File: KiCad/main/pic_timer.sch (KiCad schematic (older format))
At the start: 4 parts, among them U10 8254, U11 8259, U12 27C512, X1 1 MHz

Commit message: Updated graphics adapter and main schematics + board.
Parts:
- added R5: 4K7, Resistor_THT:R_Axial_DIN0207_L6.3mm_D2.5mm_P7.62mm_Horizontal, symbol Device:R
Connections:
- net VCC: now also R5.1; no longer U11.16 (~SP~/~EN~)
- net ~IO2 renamed ~IO_DBG
- new net: R5.2, U11.16 (~SP~/~EN~)
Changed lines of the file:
@@
 ~IO1
 Text GLabel 9550 3000 2    50   Output ~ 0
-~IO2
+~IO_DBG
 Text GLabel 9900 3100 2    50   Output ~ 0
 ~VGA_MEM
@@
 Text GLabel 6000 2350 2    50   Input ~ 0
 IRQ2
-Wire Wire Line
-	5900 3150 6250 3150
 Wire Wire Line
 	6250 3150 6250 3050
@@
 NoConn ~ 5900 2850
 NoConn ~ 5900 2950
+$Comp
+L Device:R R5
+U 1 1 5F78548B
+P 6100 3150
+F 0 "R5" V 5893 3150 50  0000 C CNN
+F 1 "4K7" V 5984 3150 50  0000 C CNN
+F 2 "Resistor_THT:R_Axial_DIN0207_L6.3mm_D2.5mm_P7.62mm_Horizontal" V 6030 3150 50  0001 C CNN
+F 3 "~" H 6100 3150 50  0001 C CNN
+	1    6100 3150
+	0    1    1    0
+$EndComp
+Wire Wire Line
+	5950 3150 5900 3150
 Wire Bus Line
 	2000 5800 2000 5950

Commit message: Updated KiCad VGA board and main board.
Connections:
- net IRQ2: now also U10.13 (OUT1)
- net IRQ0: now reaches U10.10 (OUT0), U11.18 (IR0)
- net IRQ1: now reaches U11.19 (IR1)
- net IRQ1: no longer U10.13 (OUT1)
- net NMI renamed TMR2
- net ~IO0 renamed ~IO_TIMER
- net ~IO1 renamed ~IO_PIC
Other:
- note added: "I/O decoder"
- moved on the sheet: R5, U10, U11, U12, X1

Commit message: Updated main system board schematics and board.
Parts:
- removed U12: 27C512, Package_DIP:DIP-28_W15.24mm_Socket_LongPads, symbol Memory_EPROM:27C512
- added R10, R11, R12, R13, R14, R9: 10K, Resistor_THT:R_Axial_DIN0207_L6.3mm_D2.5mm_P2.54mm_Vertical, symbol Device:R_Small
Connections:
- net A2 is gone; now on net A1: U10.20 (A1)
- net A1: no longer U10.19 (A0), U11.27 (A0)
- net GND: now also R10.2, R11.2, R12.2, R13.2, R14.2, R9.2
- net IRQ1: now also R9.1
- net IRQ3: now also R10.1
- net IRQ4: now also R11.1
- net IRQ5: now also R12.1
- net IRQ6: now also R13.1
- net IRQ7: now also R14.1
- new net A0: U10.19 (A0), U11.27 (A0)
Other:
- note removed: "I/O decoder"
- moved on the sheet: R5, U10, U11, X1

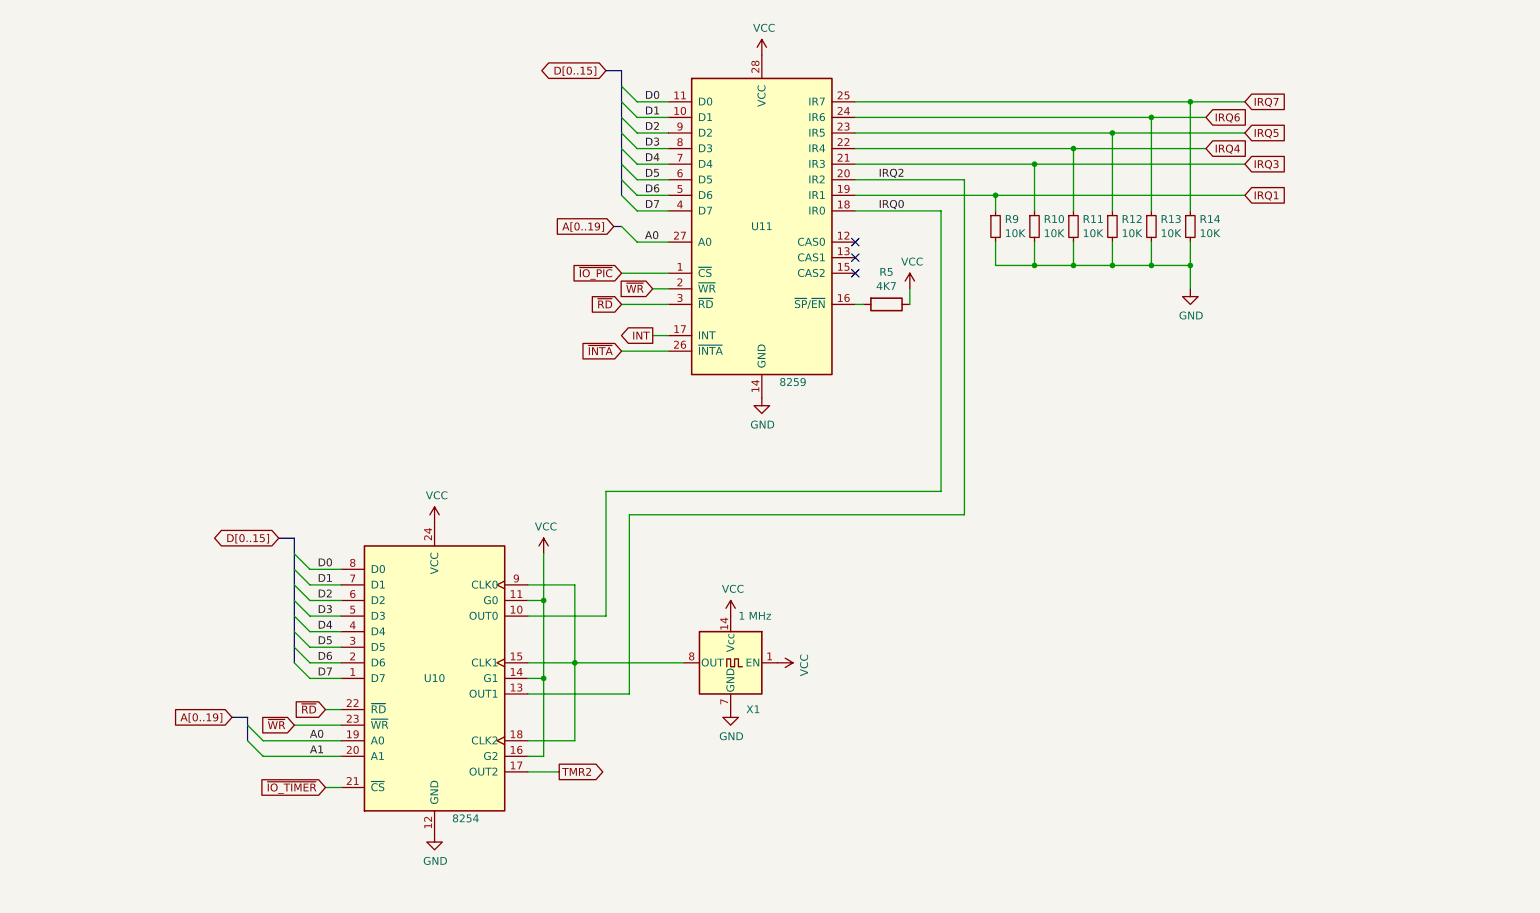
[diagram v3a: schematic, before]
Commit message: Fixed main and info_board bugs.
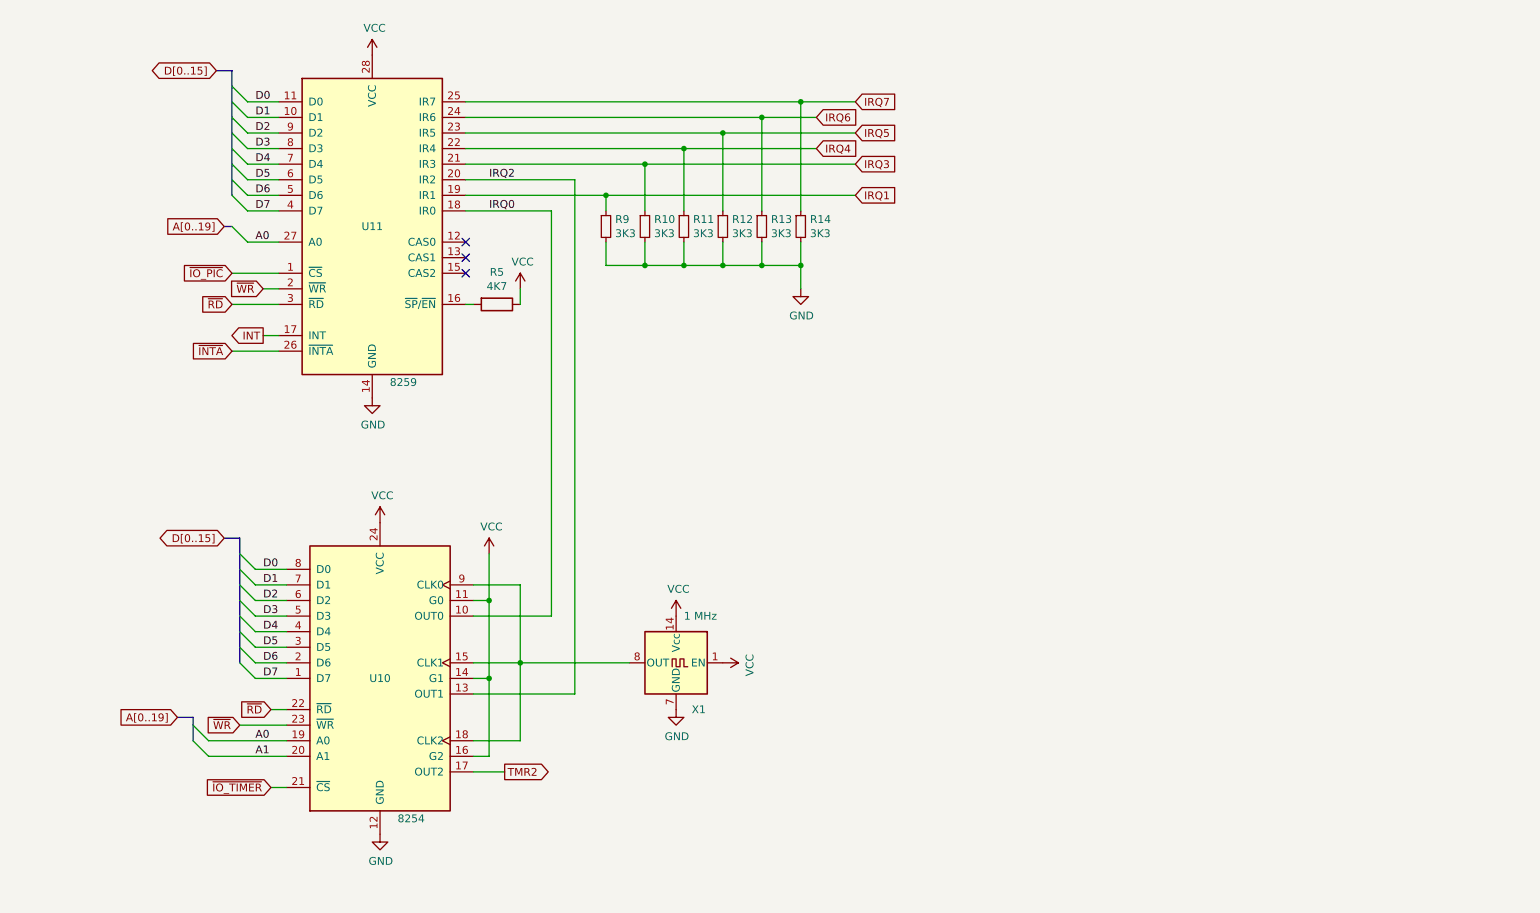
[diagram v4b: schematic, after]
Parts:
- R10, R11, R12, R13, R14, R9: value 10K -> 3K3
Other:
- moved on the sheet: R10, R11, R12, R13, R14, R5, R9, U10, U11, X1
